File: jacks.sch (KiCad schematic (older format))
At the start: 78 parts, among them J1 PJ301CM, J10 PJ301BM, J11 PJ301BM, J12 PJ301BM, J13 PJ301BM, J14 PJ301BM, J15 PJ301BM, J16 PJ301BM, J17 PJ301BM, J18 PJ301BM, J19 PJ301BM, J2 PJ301CM, J20 PJ301BM, J21 PJ301BM, J22 PJ301BM, J23 PJ301BM, J24 PJ301BM, J25 PJ301BM, J26 PJ301BM, J3 PJ301BM, J4 PJ301BM, J5 PJ301BM, J6 PJ301BM, J7 PJ301BM, J8 PJ301BM, J9 PJ301BM, Q1 MMBT3904, Q2 MMBT3904, Q3 MMBT3904, Q4 MMBT3904, U1 VO0600T, U2 74LV1T34, U6 MCP6004

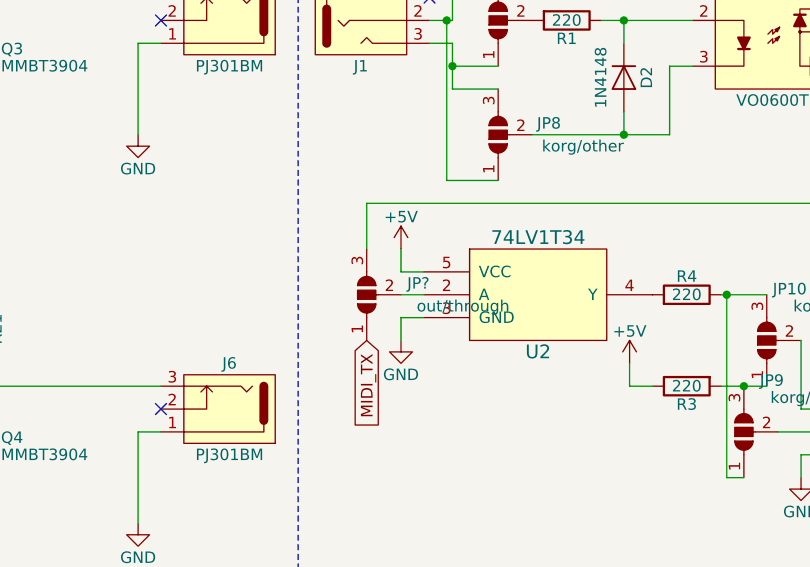
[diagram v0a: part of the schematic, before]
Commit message: Fixed LCSC values.
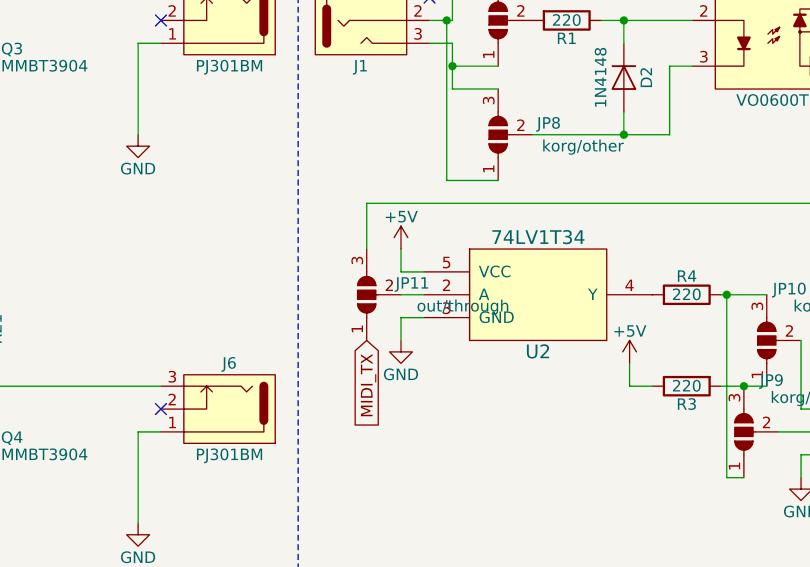
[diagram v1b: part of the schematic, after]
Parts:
- R14: LCSC (none) -> C25803
- gave numbers to parts that had none: 1
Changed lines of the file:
@@
 EESchema Schematic File Version 4
-LIBS:sequencer-cache
 EELAYER 30 0
 EELAYER END
@@
 F 5 "ERJ-3EKF1003V" H 1530 1800 50  0001 C CNN "MFP"
 F 6 "0603" H 1530 1800 50  0001 C CNN "Package"
+F 7 "C25803" V 1450 1700 50  0001 C CNN "LCSC"
 	1    1450 1700
 	0    1    1    0
@@
 korg: ring=5V tip=signal\n-> jp pos 2-3
 $Comp
-L Jumper:SolderJumper_3_Open JP?
+L Jumper:SolderJumper_3_Open JP11
 U 1 1 5F1CCD60
 P 5700 2700
-F 0 "JP?" V 5750 2425 50  0000 L CNN
+F 0 "JP11" V 5750 2425 50  0000 L CNN
 F 1 "out/through" V 5650 2075 50  0000 L CNN
 F 2 "Jumper:SolderJumper-3_P1.3mm_Open_Pad1.0x1.5mm" H 5700 2700 50  0001 C CNN
